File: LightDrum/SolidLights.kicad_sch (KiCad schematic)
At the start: 11 parts, among them U12 NCR420PAS, U13 NCR420PAS, U14 NCR420PAS, U15 INA180A3

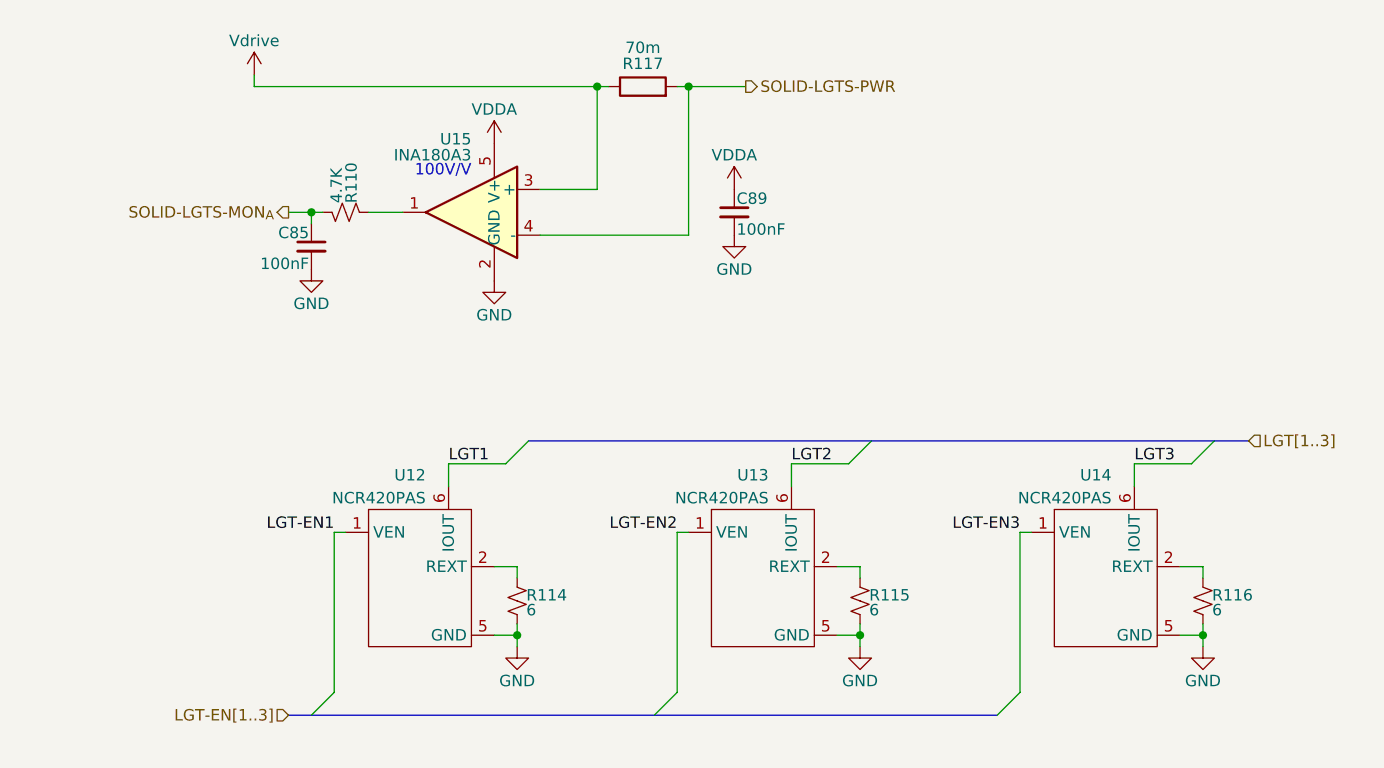
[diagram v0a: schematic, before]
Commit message: Organize old files and generate interface gerbers
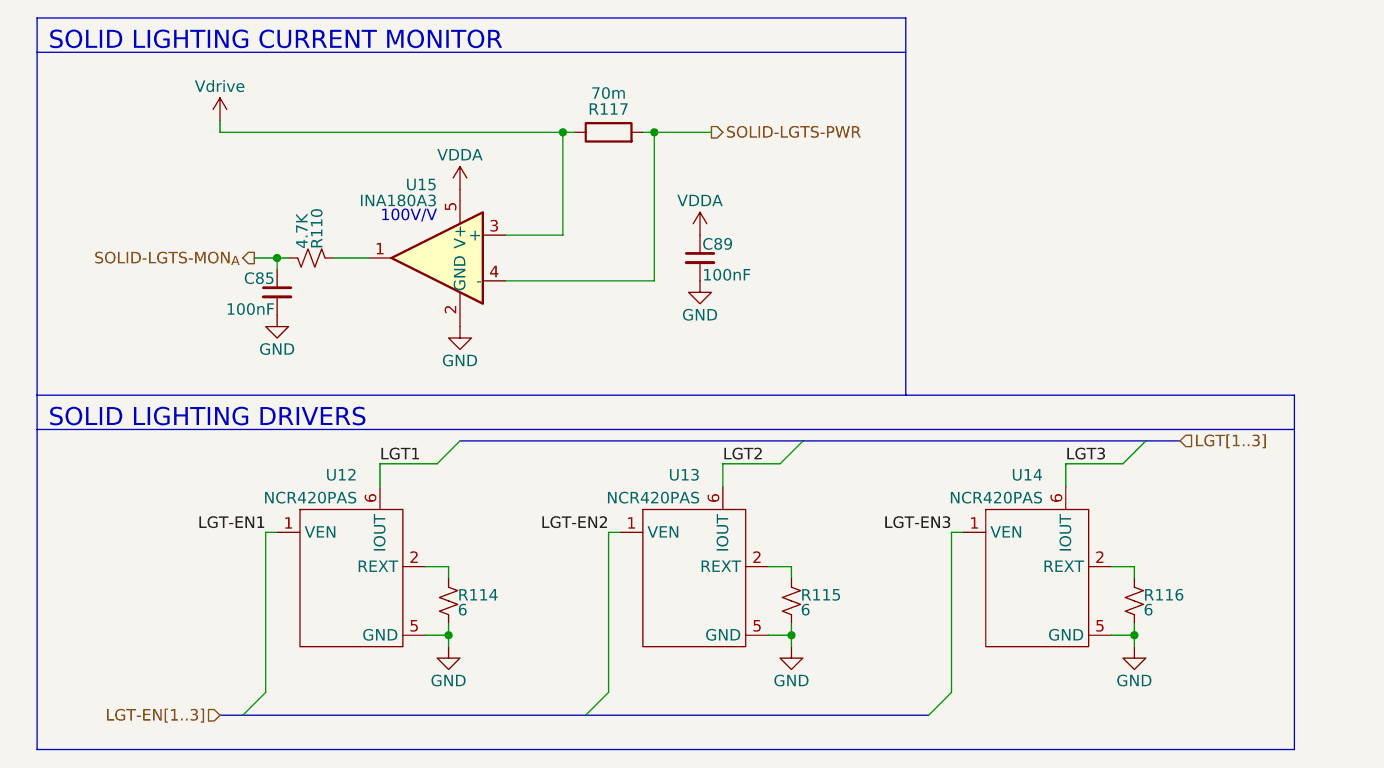
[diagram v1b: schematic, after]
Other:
- note added: "SOLID LIGHTING CURRENT MONITOR"
- note added: "SOLID LIGHTING DRIVERS"
- moved on the sheet: C85, C89, R110, R114, R115, R116, R117, U12, U13, U14, U15

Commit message: (WIP) REV12 Testing and firmware dev
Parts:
- R117: value 70m -> 150m
- U15: value INA180A3 -> INA180A2
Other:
- note added: "50V/V"
- note removed: "100V/V"
- company: (none) -> Daxxn Industries
- title: (none) -> LightDrum
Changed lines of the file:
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@@
 (kicad_sch (version 20230121) (generator eeschema)
   (paper "A4")
+  (title_block
+    (title "LightDrum")
+    (rev "REV13")
+    (company "Daxxn Industries")
+  )
   (junction (at 134.62 81.28) (diameter 0) (color 0 0 0 0)
   )
@@
     (stroke (width 0) (type default))
   )
-  (text "100V/V" (at 57.15 35.56 0)
+  (text "50V/V" (at 57.15 35.56 0)
     (effects (font (size 1.27 1.27)) (justify right bottom))
   )
@@
       (effects (font (size 1.27 1.27)) (justify left))
     )
-    (property "Value" "INA180A3" (at 57.15 33.02 0)
+    (property "Value" "INA180A2" (at 57.15 33.02 0)
       (effects (font (size 1.27 1.27)) (justify left))
     )
@@
       (effects (font (size 1.27 1.27)))
     )
-    (property "Value" "70m" (at 76.2 21.082 90)
-      (effects (font (size 1.27 1.27)))
-    )
+    (property "Value" "150m" (at 76.2 21.082 90)
+      (effects (font (size 1.27 1.27)))
+    )

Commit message: REV13 - Update to KiCAD 8
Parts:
- renumbered C85 to C90, R110 to R118

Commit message: REV13 - Revert to KiCAD 7
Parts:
- renumbered C90 to C85, R118 to R110
